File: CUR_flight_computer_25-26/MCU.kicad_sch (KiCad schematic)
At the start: 28 parts, among them SW1 GSPTS0018, SW2 GSPTS0018, U1 STM32H523VETx, Y1 16M18PX/XT324-10/10

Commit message: routing pyro power
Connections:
- net BATT_SENSE: now also U1.16 (PC1); no longer U1.18 (PC3)
- net I_SENSE: now also U1.15 (PC0); no longer U1.17 (PC2)
- net I_SENSE_PYRO: now also U1.17 (PC2); no longer U1.15 (PC0)
- net PYRO_BATT_SENSE: now also U1.18 (PC3); no longer U1.16 (PC1)

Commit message: Remove JTDI and combine NRST and ~{RESET}
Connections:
- net NRST is gone; now on net ~{RESET}: C5.1, SW1.1, U1.14 (NRST)
- net ~{RESET}: no longer U1.90 (PB4(NJTRST))
- net JTDI: no longer names the net of U1.77 (PA15(JTDI))
- no-connect marks 0 -> 2
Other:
- note added: "from dbg"

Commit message: Move mag CS pin to old JTDI pin
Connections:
- net MAG_CS: now also U1.77 (PA15(JTDI)); no longer U1.29 (PA4)
- no-connect marks 2 -> 1

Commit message: routed led
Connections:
- net BTN_1: now also U1.86 (PD5); no longer U1.84 (PD3)
- net BTN_3: now also U1.84 (PD3); no longer U1.86 (PD5)
- net LED_1_B: now also U1.67 (PA8); no longer U1.69 (PA10)
- net LED_1_R: now also U1.69 (PA10); no longer U1.67 (PA8)

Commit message: Update debug header and crystal
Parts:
- Y1: footprint Oscillator:Oscillator_SMD_Abracon_ASE-4Pin_3.2x2.5mm -> Crystal:Crystal_SMD_3225-4Pin_3.2x2.5mm

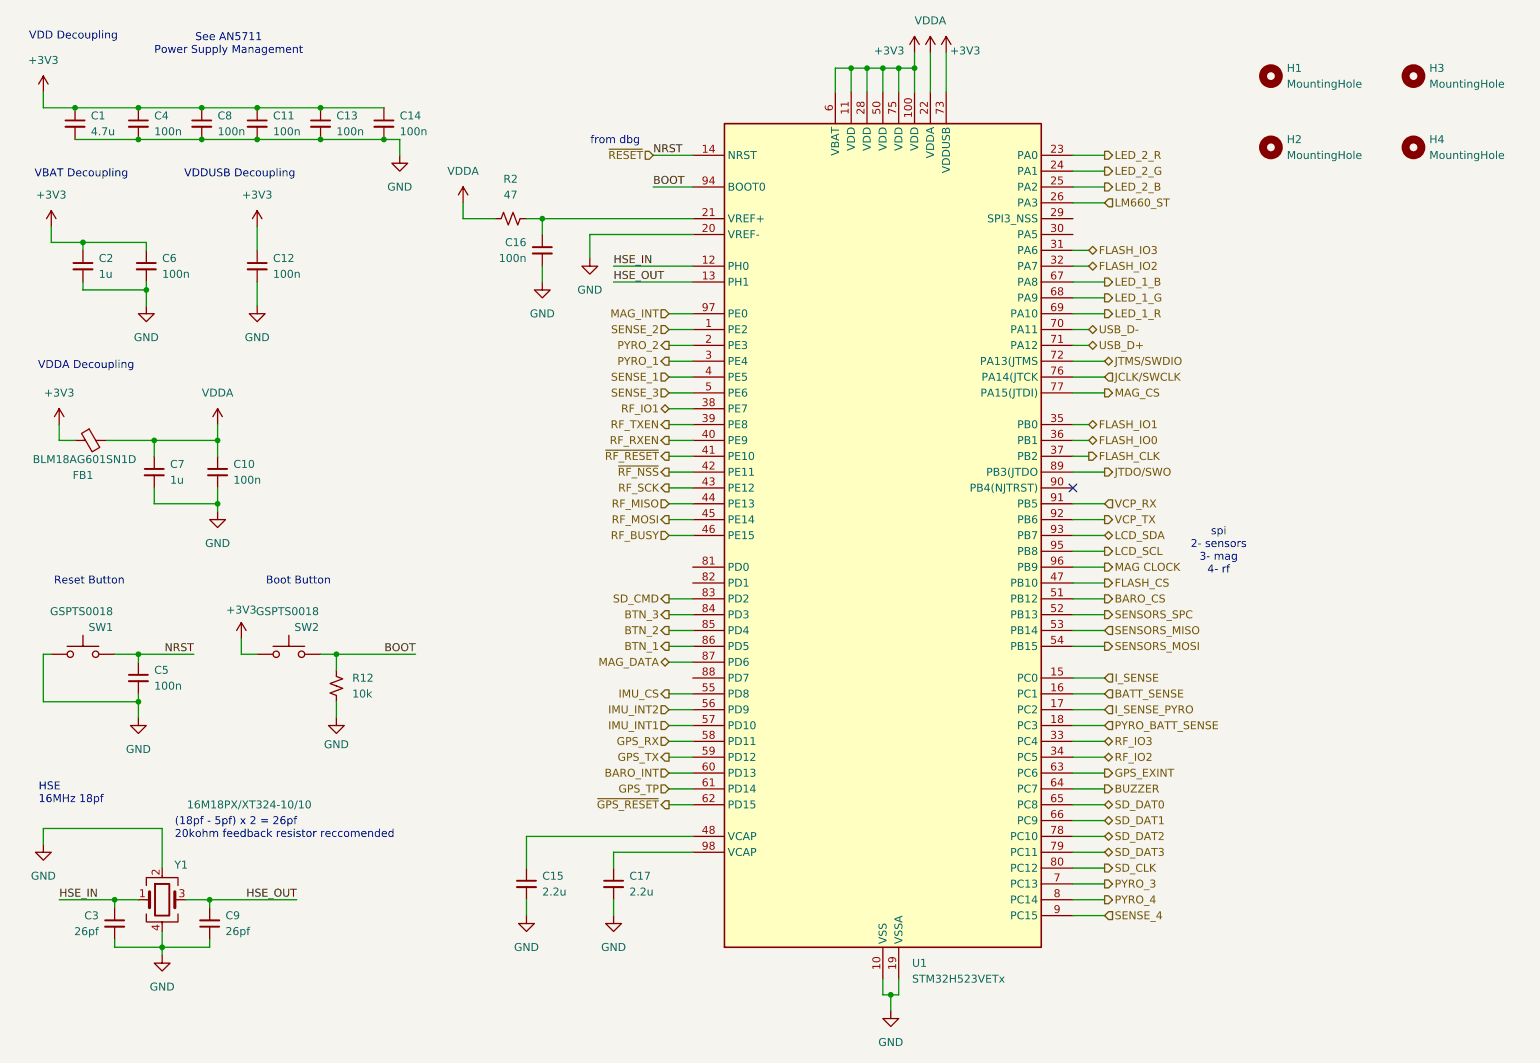
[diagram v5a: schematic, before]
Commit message: Apply MPNs for capacitors and connectors
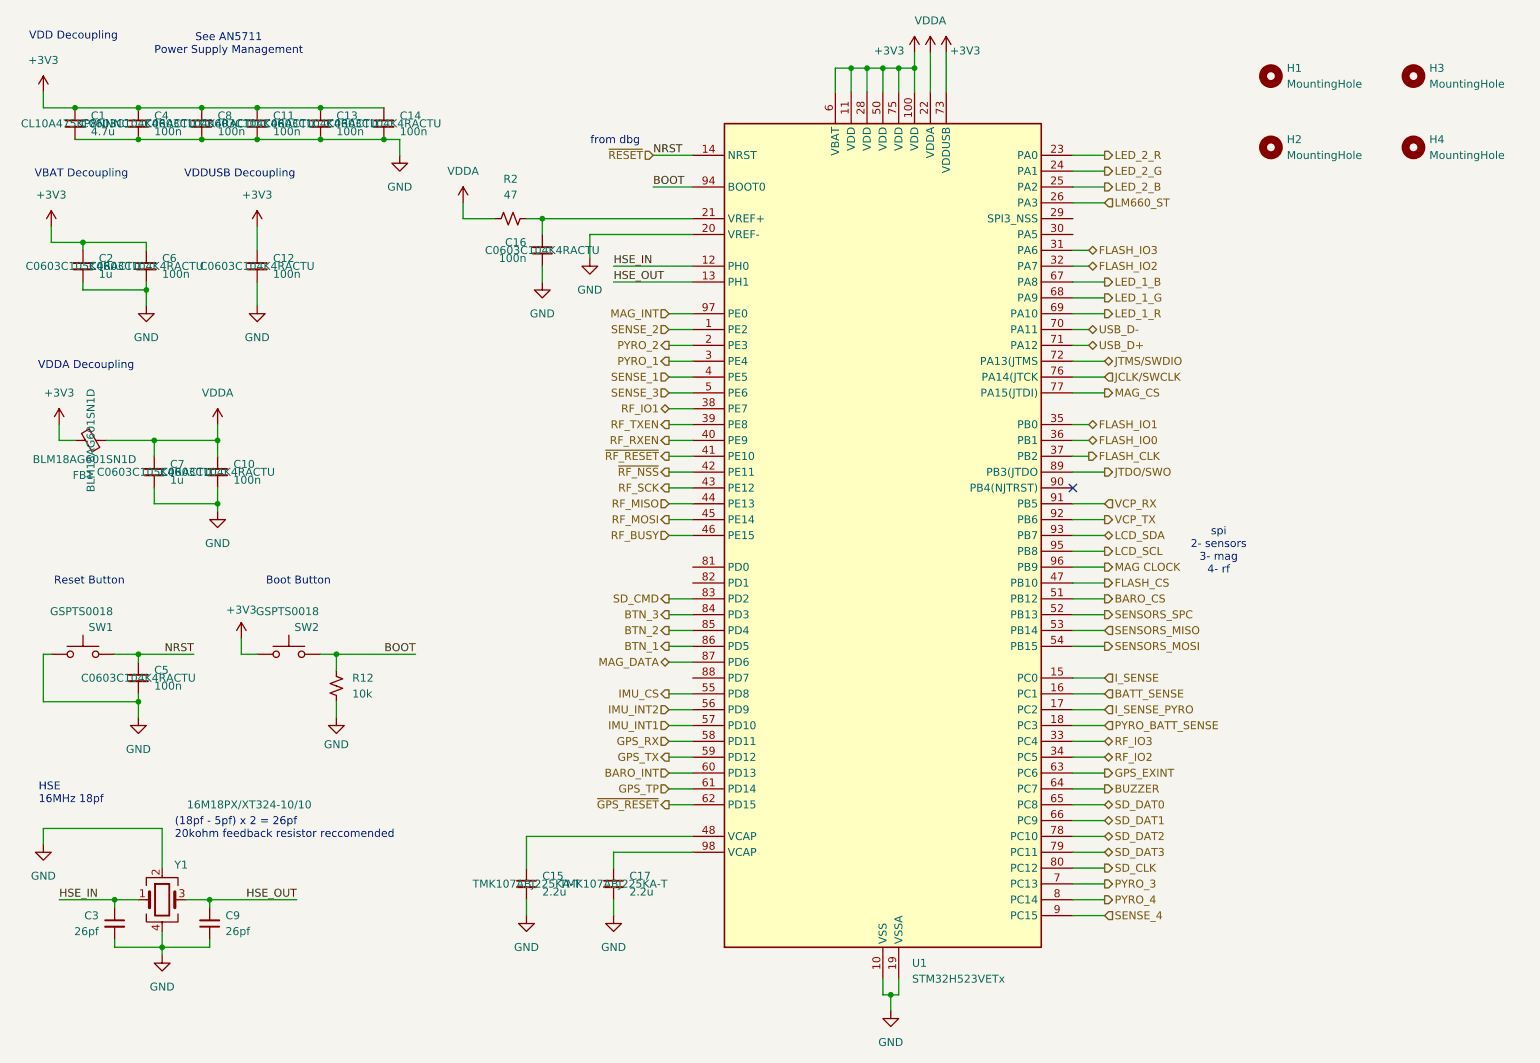
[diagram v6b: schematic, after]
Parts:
- C1: MPN (none) -> CL10A475KP8NNNC
- C10, C11, C12, C13, C14, C16, C4, C5, C6, C8: MPN (none) -> C0603C104K4RACTU
- C15, C17: MPN (none) -> TMK107ABJ225KA-T
- C2, C7: MPN (none) -> C0603C105K4RACTU
- FB1: MPN (none) -> BLM18AG601SN1D

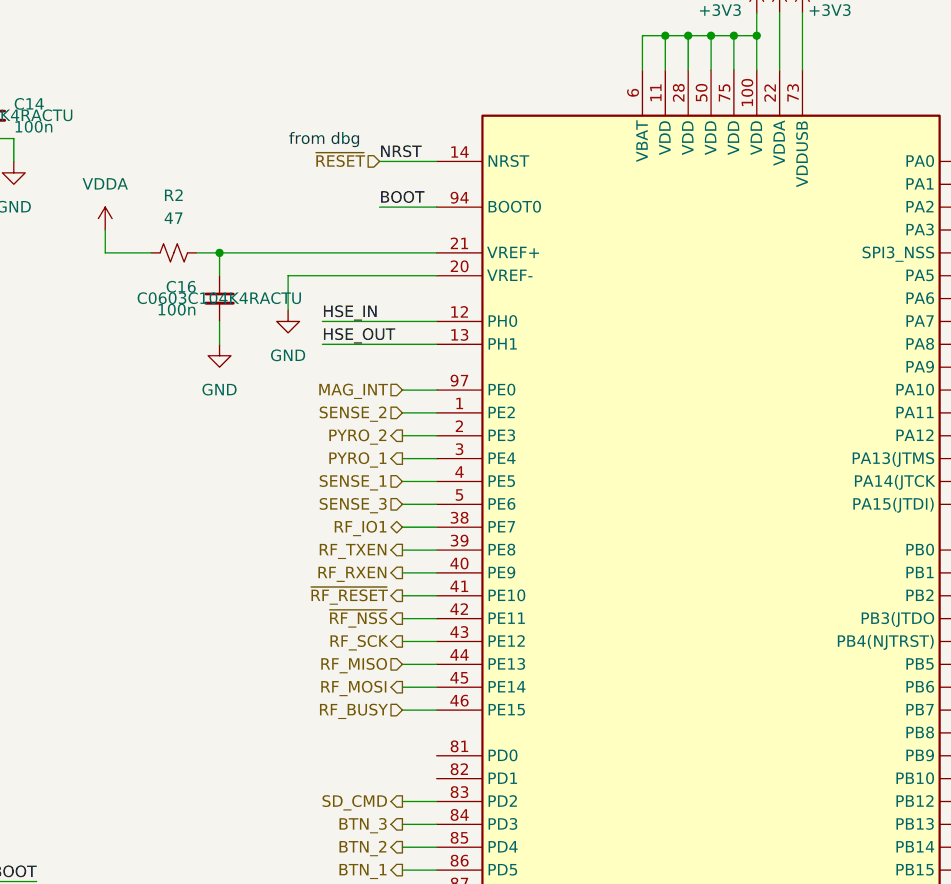
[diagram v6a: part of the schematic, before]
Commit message: Add MPNs for ICs
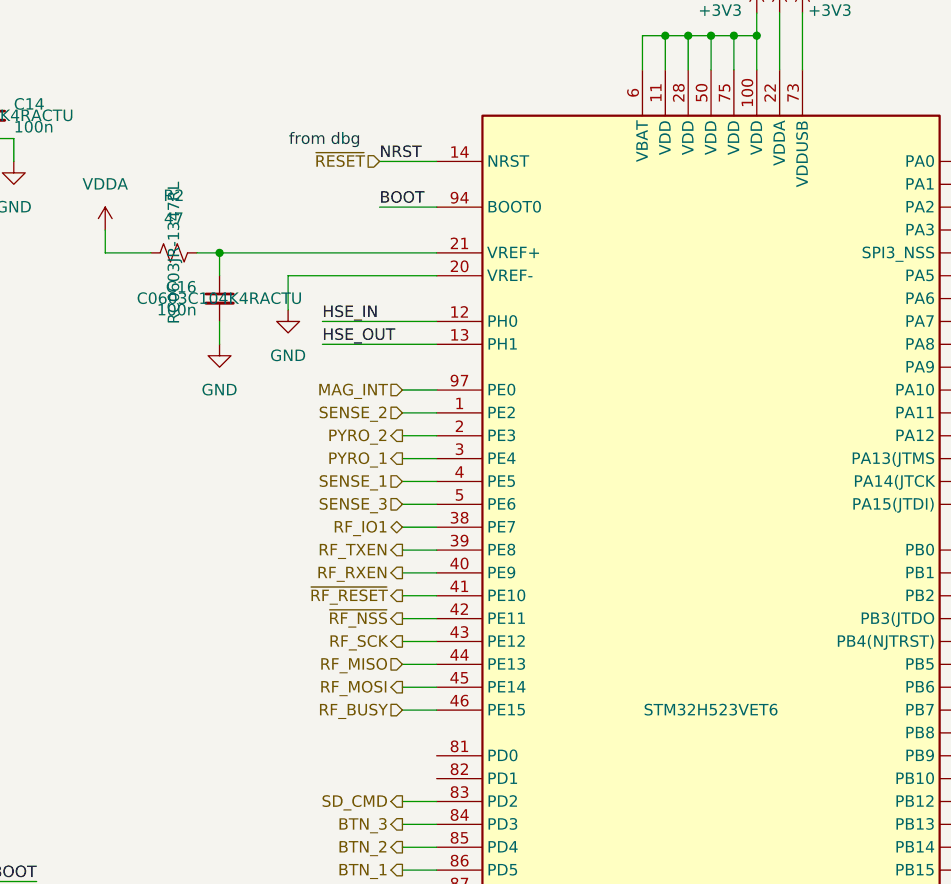
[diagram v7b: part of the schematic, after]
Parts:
- R12: MPN RC0603FR-0747KL -> RC0603FR-0710KL
- R2: MPN (none) -> RC0603JR-1347RL
- SW1, SW2: MPN SKRPADE010 -> PTS815SJG250SMTR LFS
- U1: MPN (none) -> STM32H523VET6

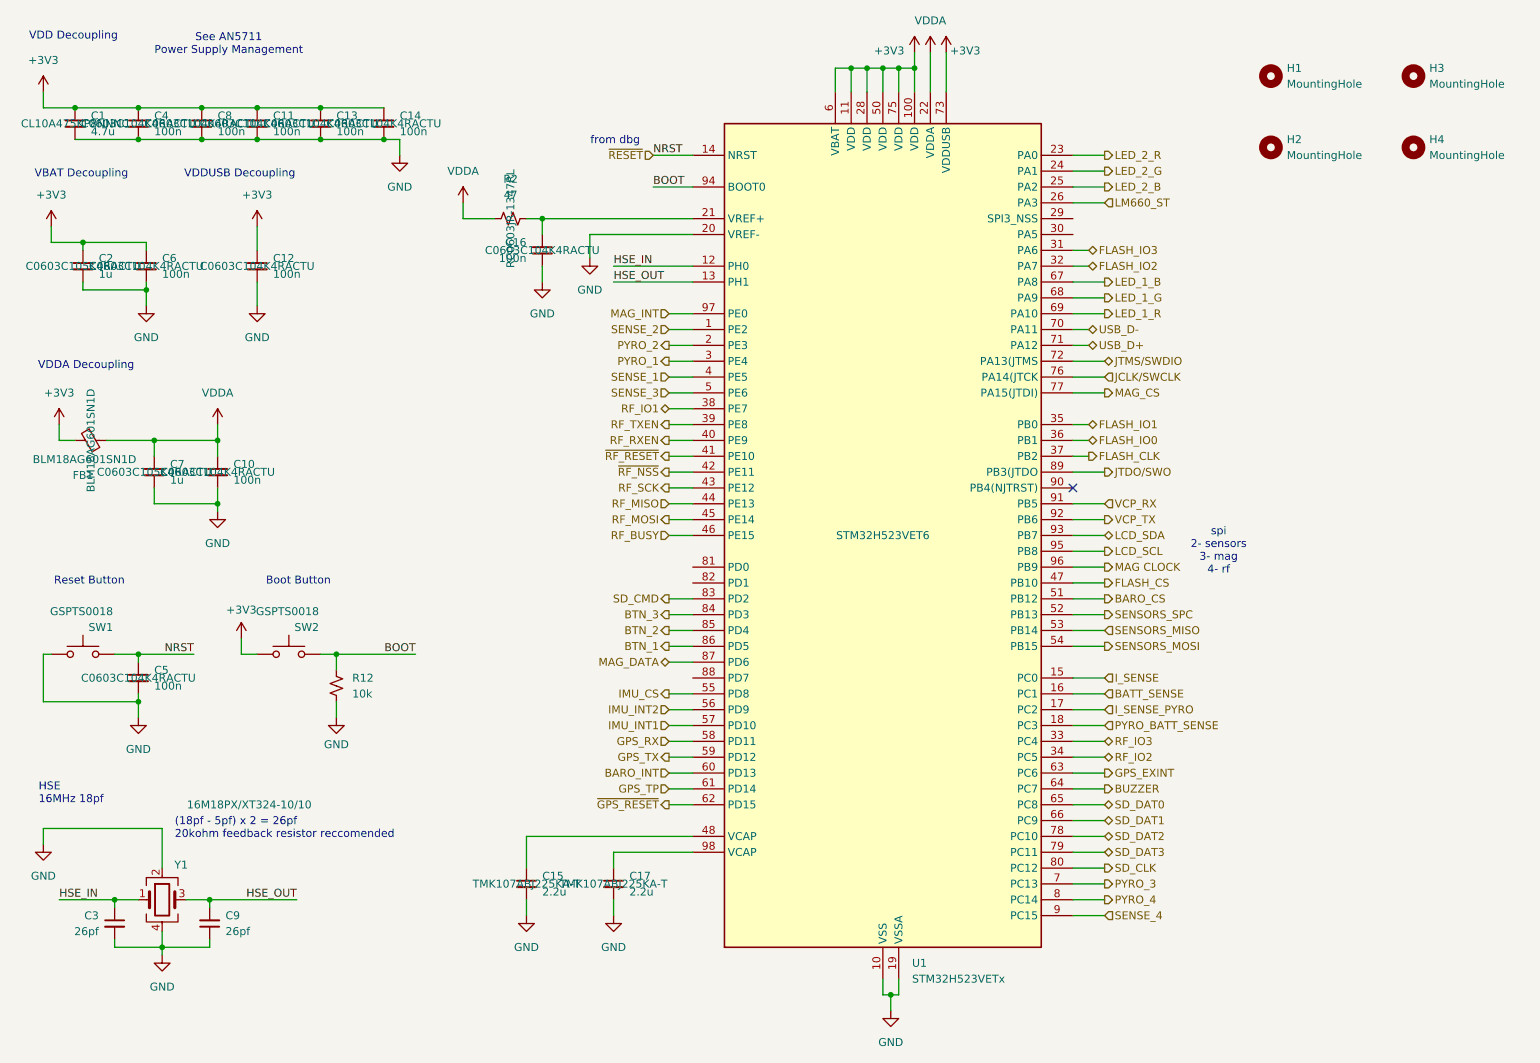
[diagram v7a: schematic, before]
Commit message: Hide MPNs
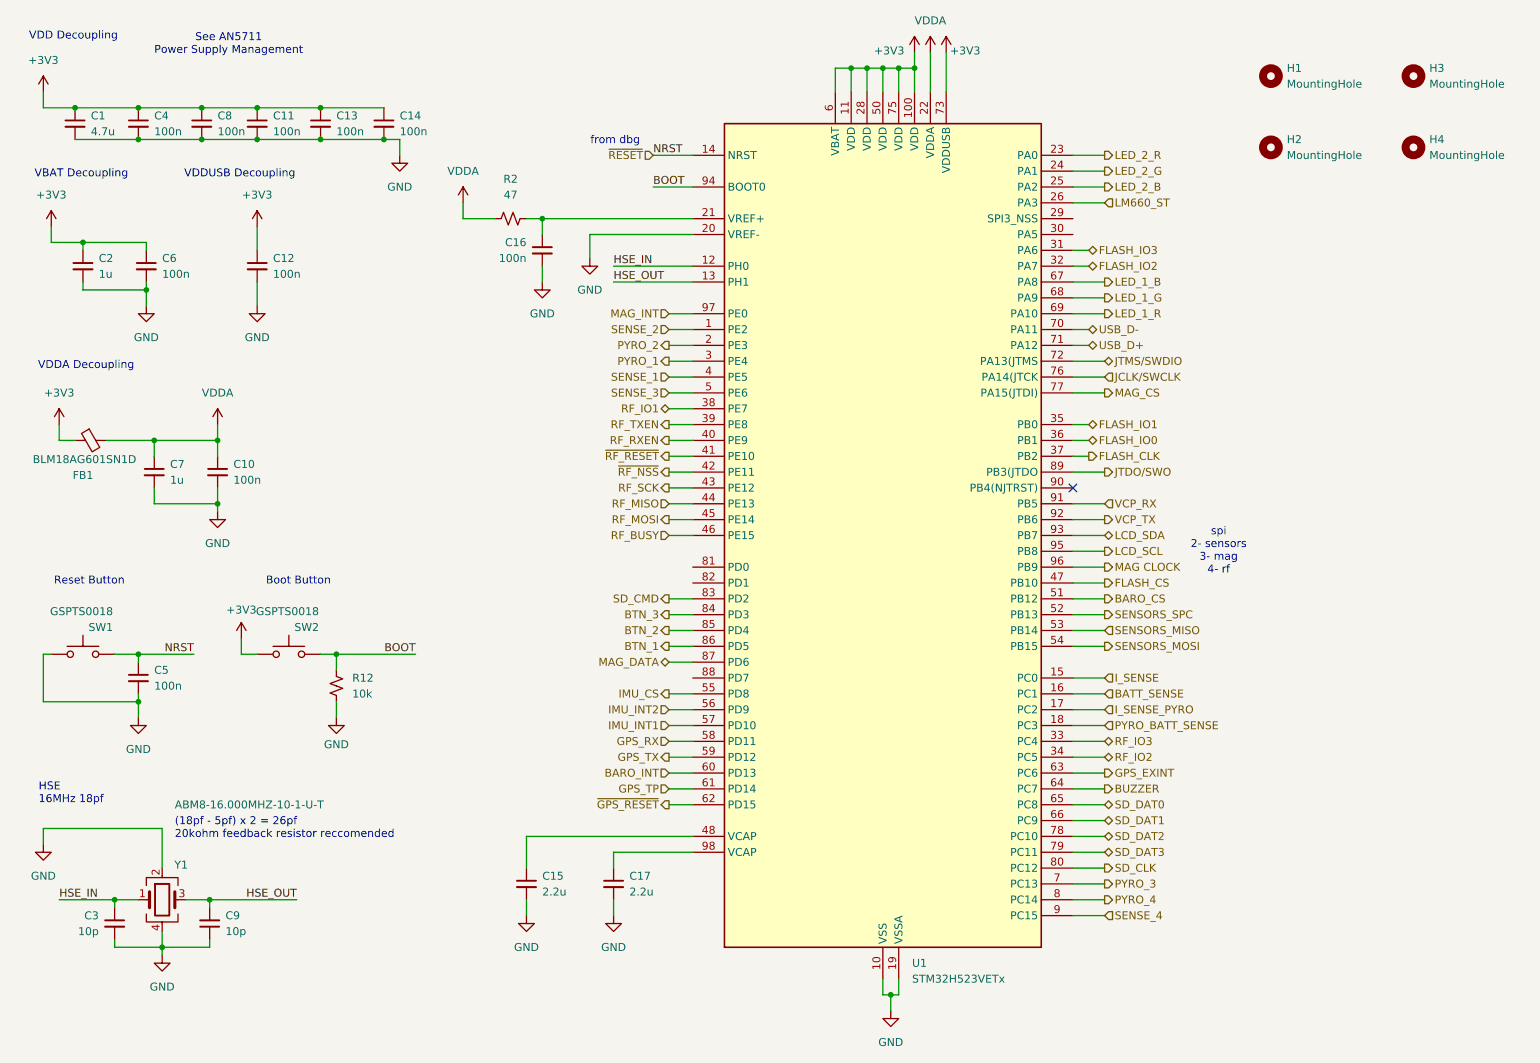
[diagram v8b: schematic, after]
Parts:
- C3, C9: value 26pf -> 10p; MPN (none) -> 0603N100J500CT
- Y1: value 16M18PX/XT324-10/10 -> ABM8-16.000MHZ-10-1-U-T; MPN (none) -> ABM8-16.000MHZ-10-1-U-T
